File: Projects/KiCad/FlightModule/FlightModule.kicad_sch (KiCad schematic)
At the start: 56 parts, among them J1 Conn_01x05_Socket, J2 Conn_01x04_Pin, J3 Conn_01x05_Pin, J4 Conn_01x02_Pin, J5 Conn_01x02_Pin, J6 Conn_01x02_Pin, J7 Conn_01x02_Pin, J8 Conn_01x02_Pin, SW1 SW_Push, SW2 SW_Push, U1 NUCLEO-F303K8, U2 MCP2562-E-P, U3 TLP222A, U4 TLP222A, U5 MB85RS2MT

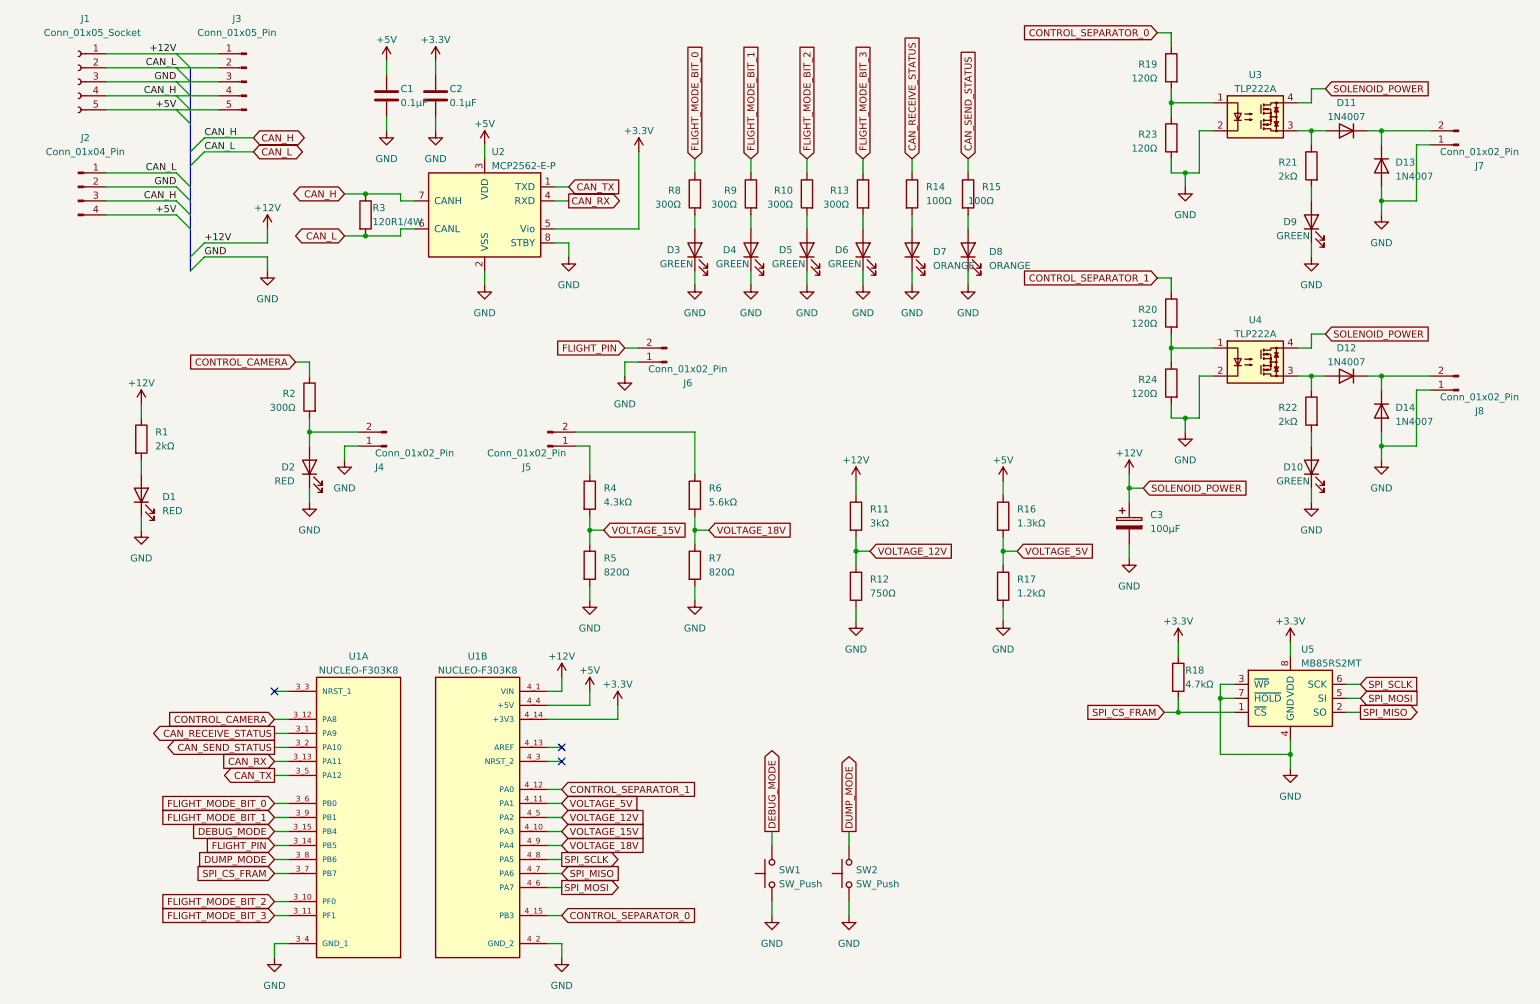
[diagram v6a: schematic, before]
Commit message: 計測モジュールとフライトモジュールのコネクタを再配置
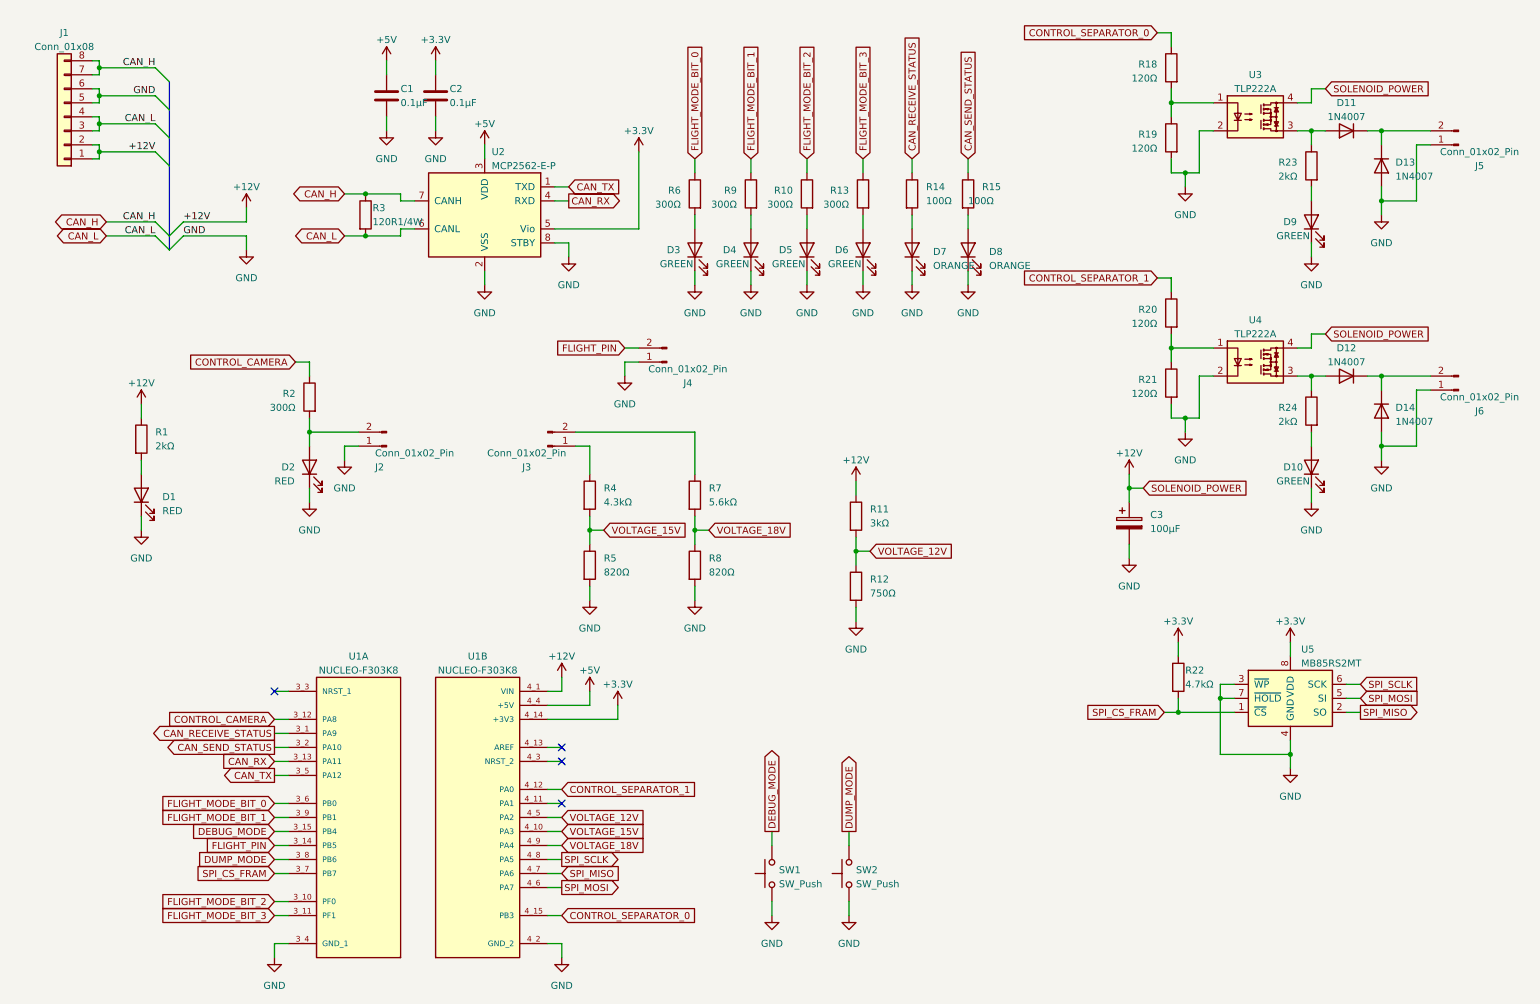
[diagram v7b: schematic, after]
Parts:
- removed J1: Conn_01x05_Socket, Connector_PinSocket_2.54mm:PinSocket_1x05_P2.54mm_Vertical, symbol Connector:Conn_01x05_Socket
- removed J2: Conn_01x04_Pin, Connector_JST:JST_XH_S4B-XH-A_1x04_P2.50mm_Horizontal, symbol Connector:Conn_01x04_Pin
- removed J3: Conn_01x05_Pin, Connector_PinHeader_2.54mm:PinHeader_1x05_P2.54mm_Vertical, symbol Connector:Conn_01x05_Pin
- removed R16: 1.3kΩ, Resistor_SMD:R_0603_1608Metric_Pad0.98x0.95mm_HandSolder, symbol Device:R
- removed R17: 1.2kΩ, Resistor_SMD:R_0603_1608Metric_Pad0.98x0.95mm_HandSolder, symbol Device:R
- added J1: Conn_01x08, Connector_Hirose:Hirose_DF11-8DP-2DSA_2x04_P2.00mm_Vertical, symbol Connector_Generic:Conn_01x08
- renumbered J4 to J2, J5 to J3, J6 to J4, J7 to J5, J8 to J6, R19 to R18, R23 to R19, R24 to R21, R18 to R22, R21 to R23, R22 to R24, R8 to R6, R6 to R7, R7 to R8
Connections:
- net +12V: now also J1.1 (Pin_1), J1.2 (Pin_2)
- net CAN_H: now also J1.7 (Pin_7), J1.8 (Pin_8)
- net CAN_L: now also J1.3 (Pin_3), J1.4 (Pin_4)
- net GND: now also J1.5 (Pin_5), J1.6 (Pin_6)
- net VOLTAGE_5V: no longer names the net of U1.4_11 (PA1)
- no-connect marks 3 -> 4

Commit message: 基板設計の都市伝説をいろいろ適応
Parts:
- renumbered C2 to C1, C1 to C2, D8 to D1, D2 to D10, D6 to D11, D5 to D12, D3 to D13, D4 to D14, D7 to D2, D10 to D3, D9 to D4, D1 to D5, D11 to D6, D13 to D7, D14 to D8, D12 to D9, J4 to J2, J6 to J4, J2 to J6, R3 to R1, R1 to R10, R24 to R11, R23 to R12, R2 to R13, R21 to R14, R20 to R15, R22 to R16, R18 to R17, R10 to R18, R13 to R19, R8 to R2, R19 to R20, R6 to R21, R9 to R22, R4 to R3, R7 to R4, R14 to R5, R15 to R6, R5 to R7, R12 to R8, R11 to R9, SW2 to SW1, SW1 to SW2, U2 to U1, U1 to U2, U4 to U3, U3 to U4
